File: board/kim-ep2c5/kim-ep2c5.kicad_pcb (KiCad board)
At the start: 2 copper layers, 84 x 54 mm, 4 parts, among them J101 Conn_02x20_Odd_Even, J102 Conn_01x16_Male, J103 TTY, U101 EP2C5

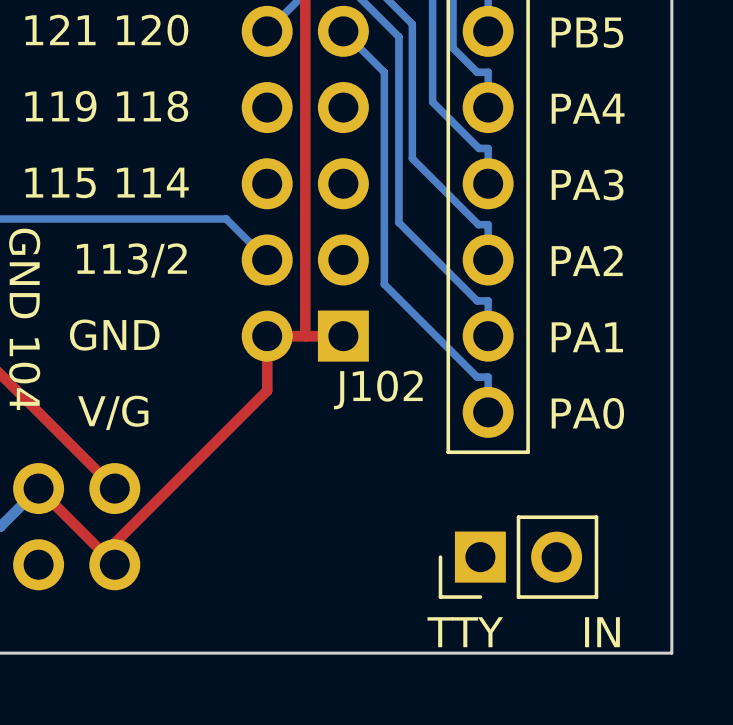
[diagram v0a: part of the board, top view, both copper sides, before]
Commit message: Added the serial connection -- oops.
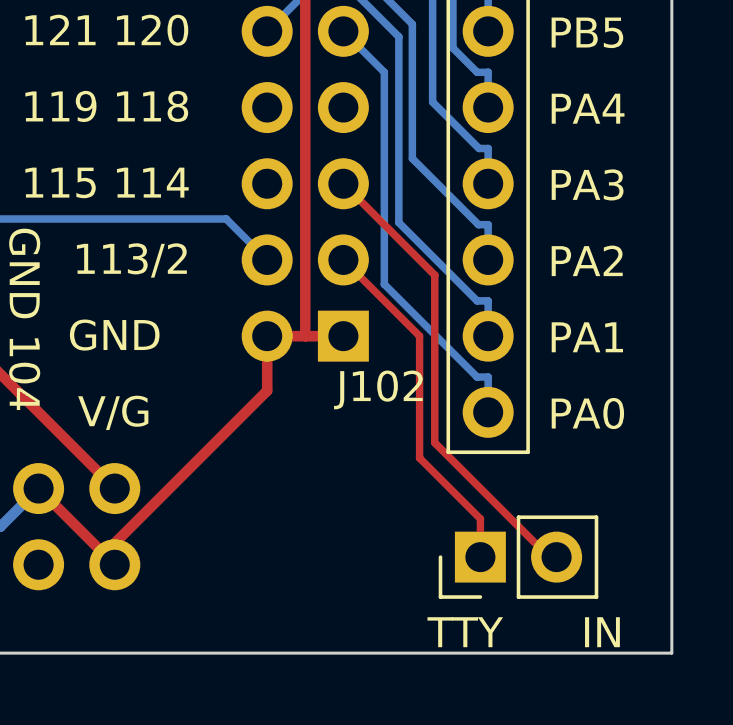
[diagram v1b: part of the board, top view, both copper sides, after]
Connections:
- U101 pad 203: unconnected-(U101-Pad203) -> TTYO
- U101 pad 205: unconnected-(U101-Pad205) -> TTYIN
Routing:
- net TTYIN: track 0.00 -> 15.5 mm
- net TTYO: track 0.00 -> 11.8 mm
